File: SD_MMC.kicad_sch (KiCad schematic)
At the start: 6 parts, among them J2 Micro_SD_Card

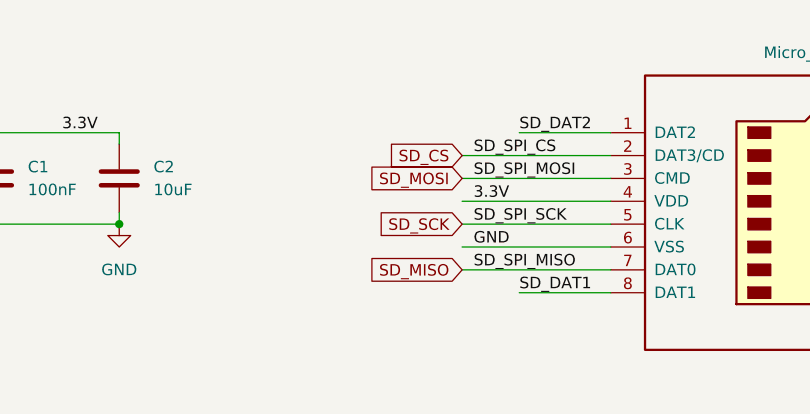
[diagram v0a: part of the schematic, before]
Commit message: Changed power regulators, filled out DRAM, begin changing FPGA from ECP5 to ICE40
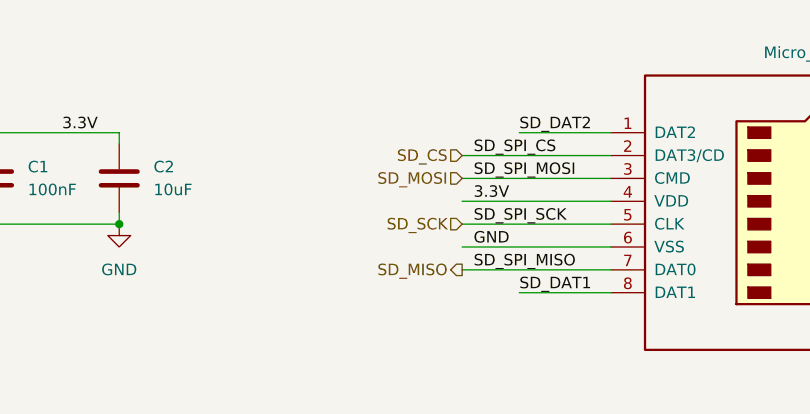
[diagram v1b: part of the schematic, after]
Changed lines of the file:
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@@
-		)
-	)
-	(global_label "SD_SCK"
-		(shape input)
-		(at 165.1 57.15 180)
-		(fields_autoplaced yes)
-		(effects
-			(font
-				(size 1.27 1.27)
-			)
-			(justify right)
-		)
-		(property "Intersheetrefs" "${INTERSHEET_REFS}"
-			(at 154.9182 57.15 0)
-			(effects
-				(font
-					(size 1.27 1.27)
-				)
-				(justify right)
-				(hide yes)
-			)
-		)
-	)
-	(global_label "SD_MISO"
-		(shape input)
-		(at 165.1 62.23 180)
-		(fields_autoplaced yes)
-		(effects
-			(font
-				(size 1.27 1.27)
-			)
-			(justify right)
-		)
-		(property "Intersheetrefs" "${INTERSHEET_REFS}"
-			(at 154.0715 62.23 0)
-			(effects
-				(font
-					(size 1.27 1.27)
-				)
-				(justify right)
-				(hide yes)
-			)
 		)
 	)
@@
 		)
 	)
-	(global_label "SD_MOSI"
+	(hierarchical_label "SD_SCK"
 		(shape input)
-		(at 165.1 52.07 180)
-		(fields_autoplaced yes)
+		(at 165.1 57.15 180)
 		(effects
 			(font
@@
 			(justify right)
 		)
-		(property "Intersheetrefs" "${INTERSHEET_REFS}"
-			(at 154.0715 52.07 0)
-			(effects
-				(font
-					(size 1.27 1.27)
-				)
-				(justify right)
-				(hide yes)
-			)
-		)
 	)
-	(global_label "SD_CS"
-		(shape input)
-		(at 165.1 49.53 180)
-		(fields_autoplaced yes)
+	(hierarchical_label "SD_MISO"
+		(shape output)
+		(at 165.1 62.23 180)
 		(effects
 			(font
@@
 			(justify right)
 		)
-		(property "Intersheetrefs" "${INTERSHEET_REFS}"
-			(at 156.1882 49.53 0)
-			(effects
-				(font
-					(size 1.27 1.27)
-				)
-				(justify right)
-				(hide yes)
+	)
+	(hierarchical_label "SD_MOSI"
+		(shape input)
+		(at 165.1 52.07 180)
+		(effects
+			(font
+				(size 1.27 1.27)
 			)
+			(justify right)
 		)
 	)
+	(hierarchical_label "SD_CS"
+		(shape input)
+		(at 165.1 49.53 180)
+		(effects
+			(font
+				(size 1.27 1.27)
+			)
+			(justify right)
+		)
+	)

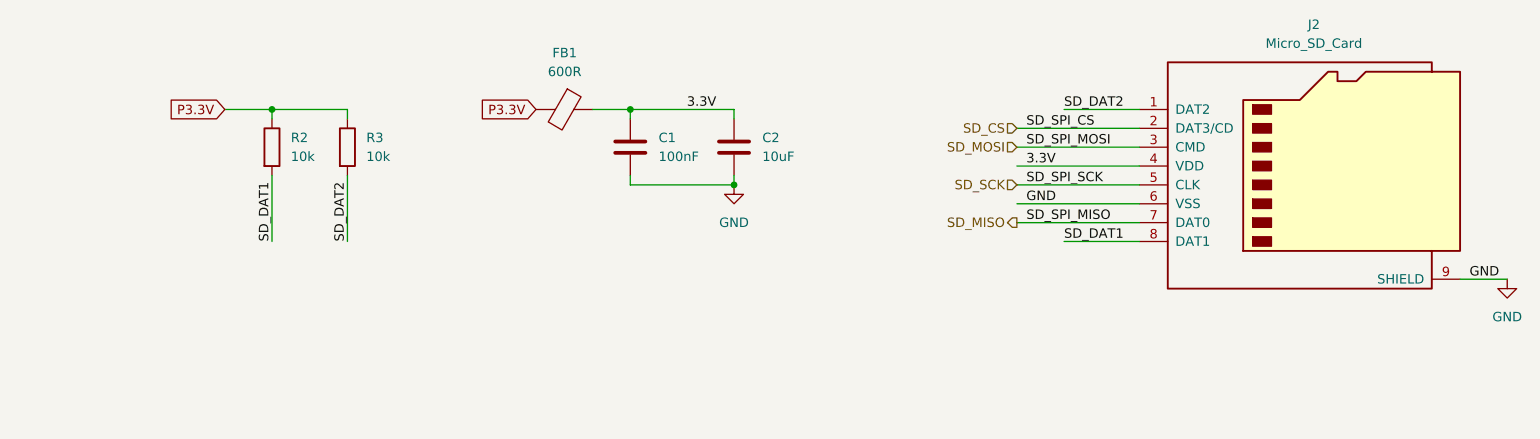
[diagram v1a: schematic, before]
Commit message: Saving before changing RAM from DDR3 to Parallel SDR SRAM
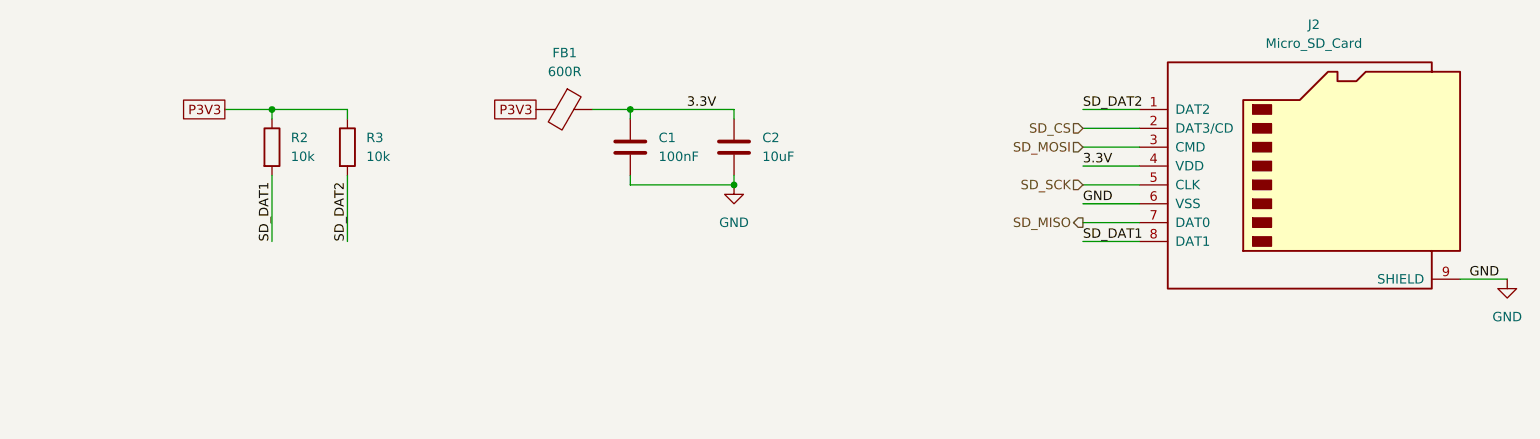
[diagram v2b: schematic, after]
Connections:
- net P3.3V renamed P3V3
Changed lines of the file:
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@@
 	(wire
 		(pts
-			(xy 165.1 57.15) (xy 181.61 57.15)
+			(xy 173.99 57.15) (xy 181.61 57.15)
 		)
 		(stroke
@@
 	(wire
 		(pts
-			(xy 165.1 54.61) (xy 181.61 54.61)
+			(xy 173.99 54.61) (xy 181.61 54.61)
 		)
 		(stroke
@@
 	(wire
 		(pts
-			(xy 165.1 62.23) (xy 181.61 62.23)
-		)
-		(stroke
-			(width 0)
-			(type default)
-		)
-	)
-	(wire
-		(pts
-			(xy 165.1 52.07) (xy 181.61 52.07)
+			(xy 173.99 62.23) (xy 181.61 62.23)
+		)
+		(stroke
+			(width 0)
+			(type default)
+		)
+	)
+	(wire
+		(pts
+			(xy 173.99 52.07) (xy 181.61 52.07)
 		)
 		(stroke
@@
 	(wire
 		(pts
-			(xy 171.45 64.77) (xy 181.61 64.77)
+			(xy 173.99 64.77) (xy 181.61 64.77)
 		)
 		(stroke
@@
 	(wire
 		(pts
-			(xy 165.1 49.53) (xy 181.61 49.53)
-		)
-		(stroke
-			(width 0)
-			(type default)
-		)
-	)
-	(wire
-		(pts
-			(xy 171.45 46.99) (xy 181.61 46.99)
-		)
-		(stroke
-			(width 0)
-			(type default)
-		)
-	)
-	(wire
-		(pts
-			(xy 165.1 59.69) (xy 181.61 59.69)
+			(xy 173.99 49.53) (xy 181.61 49.53)
+		)
+		(stroke
+			(width 0)
+			(type default)
+		)
+	)
+	(wire
+		(pts
+			(xy 173.99 46.99) (xy 181.61 46.99)
+		)
+		(stroke
+			(width 0)
+			(type default)
+		)
+	)
+	(wire
+		(pts
+			(xy 173.99 59.69) (xy 181.61 59.69)
 		)
 		(stroke
@@
 		)
 	)
-	(label "SD_SPI_CS"
-		(at 166.37 49.53 0)
-		(effects
-			(font
-				(size 1.27 1.27)
-			)
-			(justify left bottom)
-		)
-	)
 	(label "SD_DAT1"
-		(at 171.45 64.77 0)
-		(effects
-			(font
-				(size 1.27 1.27)
-			)
-			(justify left bottom)
-		)
-	)
-	(label "SD_SPI_MISO"
-		(at 166.37 62.23 0)
-		(effects
-			(font
-				(size 1.27 1.27)
-			)
-			(justify left bottom)
-		)
-	)
-	(label "SD_SPI_MOSI"
-		(at 166.37 52.07 0)
+		(at 173.99 64.77 0)
 		(effects
 			(font
@@
 	)
 	(label "3.3V"
-		(at 166.37 54.61 0)
+		(at 173.99 54.61 0)
 		(effects
 			(font
@@
 	)
 	(label "GND"
-		(at 166.37 59.69 0)
+		(at 173.99 59.69 0)
 		(effects
 			(font
@@
 		)
 	)
-	(label "SD_SPI_SCK"
-		(at 166.37 57.15 0)
-		(effects
-			(font
-				(size 1.27 1.27)
-			)
-			(justify left bottom)
-		)
-	)
 	(label "SD_DAT2"
-		(at 171.45 46.99 0)
-		(effects
-			(font
-				(size 1.27 1.27)
-			)
-			(justify left bottom)
-		)
-	)
-	(global_label "P3.3V"
-		(shape input)
+		(at 173.99 46.99 0)
+		(effects
+			(font
+				(size 1.27 1.27)
+			)
+			(justify left bottom)
+		)
+	)
+	(global_label "P3V3"
+		(shape passive)
 		(at 100.33 46.99 180)
 		(fields_autoplaced yes)
@@
 		)
 		(property "Intersheetrefs" "${INTERSHEET_REFS}"
-			(at 91.9624 46.99 0)
+			(at 93.6785 46.99 0)
 			(effects
 				(font
@@
 		)
 	)
-	(global_label "P3.3V"
-		(shape input)
+	(global_label "P3V3"
+		(shape passive)
 		(at 58.42 46.99 180)
 		(fields_autoplaced yes)
@@
 		)
 		(property "Intersheetrefs" "${INTERSHEET_REFS}"
-			(at 50.0524 46.99 0)
+			(at 51.7685 46.99 0)
 			(effects
 				(font
@@
 	(hierarchical_label "SD_SCK"
 		(shape input)
-		(at 165.1 57.15 180)
+		(at 173.99 57.15 180)
 		(effects
 			(font
@@
 	(hierarchical_label "SD_MISO"
 		(shape output)
-		(at 165.1 62.23 180)
+		(at 173.99 62.23 180)
 		(effects
 			(font
@@
 	(hierarchical_label "SD_MOSI"
 		(shape input)
-		(at 165.1 52.07 180)
+		(at 173.99 52.07 180)
 		(effects
 			(font
@@
 	(hierarchical_label "SD_CS"
 		(shape input)
-		(at 165.1 49.53 180)
-		(effects
-			(font
+		(at 173.99 49.53 180)
+		(effects
+			(font

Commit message: Power routed. Saving before reworking ICE40 pins to optimize layout
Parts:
- added R45, R46, R47: 10k, Resistor_SMD:R_0603_1608Metric, symbol Device:R
- C1, C2: footprint (none) -> Capacitor_SMD:C_0603_1608Metric
- J2: footprint (none) -> Connector_Card:microSD_HC_Hirose_DM3BT-DSF-PEJS
- R2, R3: footprint (none) -> Resistor_SMD:R_0603_1608Metric
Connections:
- net P3V3: now also R45.1, R46.1, R47.1
- net SD_DAT1: now also R45.2; no longer R2.2
- net SD_CS renamed SD_DAT3
- net SD_DAT3: now also R2.2
- net SD_MISO renamed SD_DAT0
- net SD_DAT0: now also R46.2
- net SD_MOSI renamed SD_CMD
- net SD_CMD: now also R47.2
- net SD_SCK renamed SD_CLK
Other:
- moved on the sheet: J2, R2, R3

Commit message: Finished board. Added BOM
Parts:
- FB1: footprint (none) -> Capacitor_SMD:C_0603_1608Metric
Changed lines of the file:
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@@
 			)
 		)
-		(property "Footprint" ""
+		(property "Footprint" "Capacitor_SMD:C_0603_1608Metric"
 			(at 104.14 45.212 90)
 			(effects

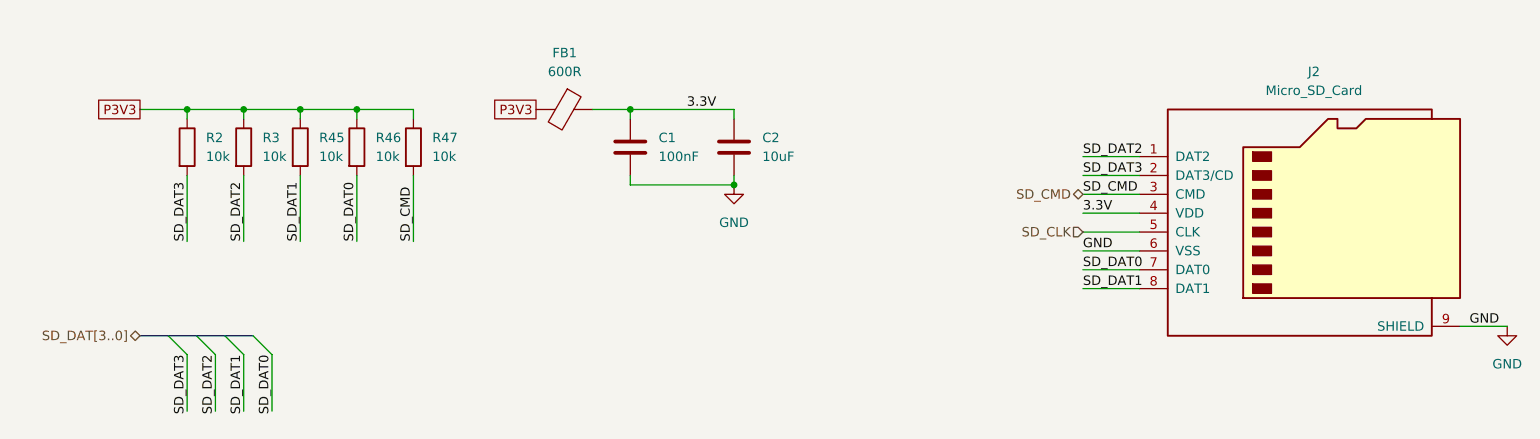
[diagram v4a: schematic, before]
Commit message: End of Version 1.0. Feedback received
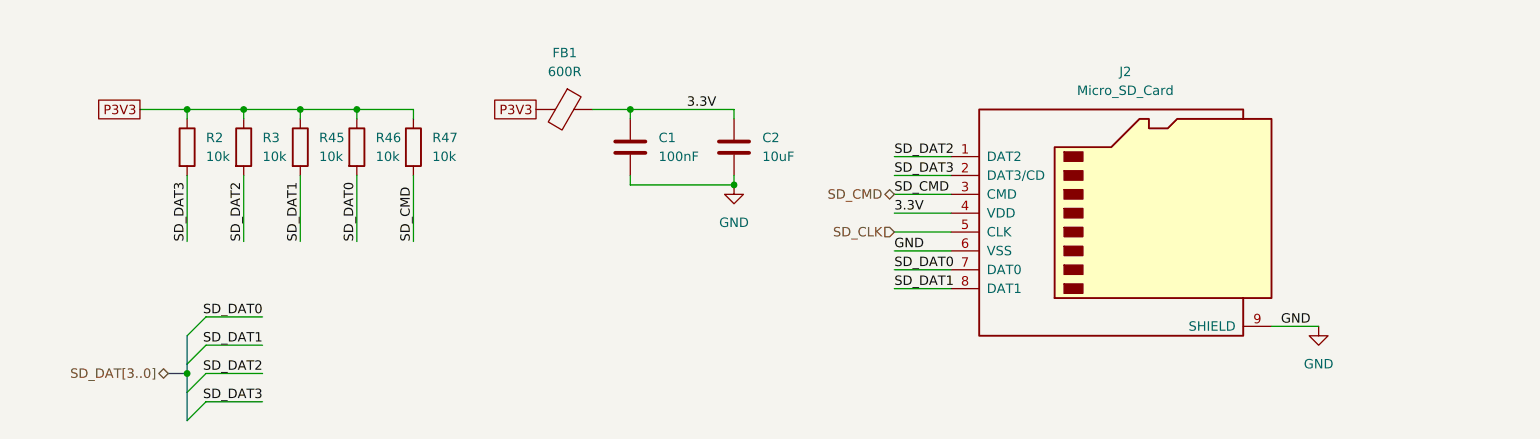
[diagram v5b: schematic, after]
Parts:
- FB1: footprint Capacitor_SMD:C_0603_1608Metric -> Inductor_SMD:L_0603_1608Metric
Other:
- moved on the sheet: J2
